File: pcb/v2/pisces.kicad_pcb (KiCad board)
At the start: 2 copper layers, 154.9 x 66 mm, 60 parts, among them J1 USB_B_Micro, J2 AudioJack4, SW1 SW_PUSH, SW10 SW_PUSH, SW11 SW_PUSH, SW12 SW_PUSH, SW13 SW_PUSH, SW14 SW_PUSH, SW15 SW_PUSH, SW16 SW_PUSH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

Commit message: Done with routing
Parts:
- moved C3 98.5 mm to (169.4, 58.1), turned to 180 degrees
- moved R2 96.2 mm to (159.1, 48.3), turned to 90 degrees
- moved R1 95.3 mm to (161.2, 48.3), turned to 90 degrees
- moved C2 90.4 mm to (158.7, 68.5)
- moved C1 89.6 mm to (158.7, 60.5), turned to 180 degrees
- moved C6 89.3 mm to (163.6, 60.5), turned to 180 degrees
- moved R3 88.7 mm to (174.0, 58.3)
- moved U1 88.6 mm to (167.7, 66.9)
- moved F1 85.0 mm to (156.8, 48.7), turned to 90 degrees
- moved C4 81.0 mm to (164.3, 58.4), turned to 180 degrees
- moved J1 76.9 mm to (160.5, 41.5), turned to 180 degrees
- moved C5 75.5 mm to (158.7, 71.4), turned to 180 degrees
- moved R4 74.1 mm to (168.8, 75.2), turned to 180 degrees
- moved Y1 50.1 mm to (157.5, 64.3), turned to 180 degrees
- moved RSTSW1 18.0 mm to (172.8, 55.4)
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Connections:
- U1 pad 10: col0 -> Net-(U1-Pad10)
- U1 pad 11: col1 -> Net-(U1-Pad11)
- U1 pad 12: col2 -> Net-(U1-Pad12)
- U1 pad 14: col3 -> row1
- U1 pad 15: col4 -> col0
- U1 pad 16: col5 -> col1
- U1 pad 17: Net-(U1-Pad17) -> col2
- U1 pad 18: Net-(U1-Pad18) -> col3
- U1 pad 19: Net-(U1-Pad19) -> col4
- U1 pad 20: Net-(U1-Pad20) -> col5
- U1 pad 21: Net-(U1-Pad21) -> col6
- U1 pad 22: Net-(U1-Pad22) -> row2
- U1 pad 23: row2 -> data
- U1 pad 25: row1 -> Net-(U1-Pad25)
- U1 pad 8: data -> Net-(U1-Pad8)
- U1 pad 9: col6 -> Net-(U1-Pad9)
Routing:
- net col0: track 53.1 -> 196.1 mm
- net col1: track 53.3 -> 177.6 mm
- net col2: track 53.3 -> 158.5 mm
- net col3: track 53.6 -> 140.1 mm
- net VCC: track 0.00 -> 79.0 mm, vias 0 -> 2
- net col4: track 53.3 -> 122.4 mm
- net col5: track 53.6 -> 104.3 mm
- net GND: track 0.00 -> 48.1 mm, vias 0 -> 1
- net col6: track 4.96 -> 38.4 mm
- net data: track 0.00 -> 30.0 mm, vias 0 -> 1
- net row2: track 131.1 -> 161.0 mm
- net row1: track 109.7 -> 137.7 mm
- net row0: track 109.7 -> 131.1 mm, vias 6 -> 7
- net d_m: track 0.00 -> 16.5 mm
- net d_p: track 0.00 -> 15.9 mm
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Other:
- board size 154.9 x 66 mm -> 138.4 x 61 mm

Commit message: PCB almost there...
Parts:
- added RR1: 10k, Resistor_SMD:R_0805_2012Metric_Pad1.20x1.40mm_HandSolder, F.Cu at (162.2, 75.2)
- moved R4 2.35 mm to (166.4, 75.2)
- moved J1 0.25 mm to (160.5, 41.7)
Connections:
- U1 pad 23: data -> Net-(U1-Pad23)
- U1 pad 8: Net-(U1-Pad8) -> data
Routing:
- net data: track 30.0 -> 38.6 mm, vias 1 -> 2
- net GND: track 48.1 -> 54.8 mm, vias 1 -> 3
- net Net-(RR1-Pad1): track 0.00 -> 6.42 mm
- net col0: track 196.1 -> 190.4 mm
- net col1: track 177.6 -> 172.0 mm
- net row1: track 137.7 -> 132.7 mm
- net col6: track 38.4 -> 34.1 mm
- net col5: track 104.3 -> 100.2 mm
- net col2: track 158.5 -> 154.6 mm
- net col4: track 122.4 -> 118.5 mm
- net col3: track 140.1 -> 136.3 mm
- net Net-(J2-PadS): track 6.53 -> 7.58 mm
- net row2: track 161.0 -> 160.2 mm
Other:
- board size 138.4 x 61 mm -> 137.8 x 60.1 mm

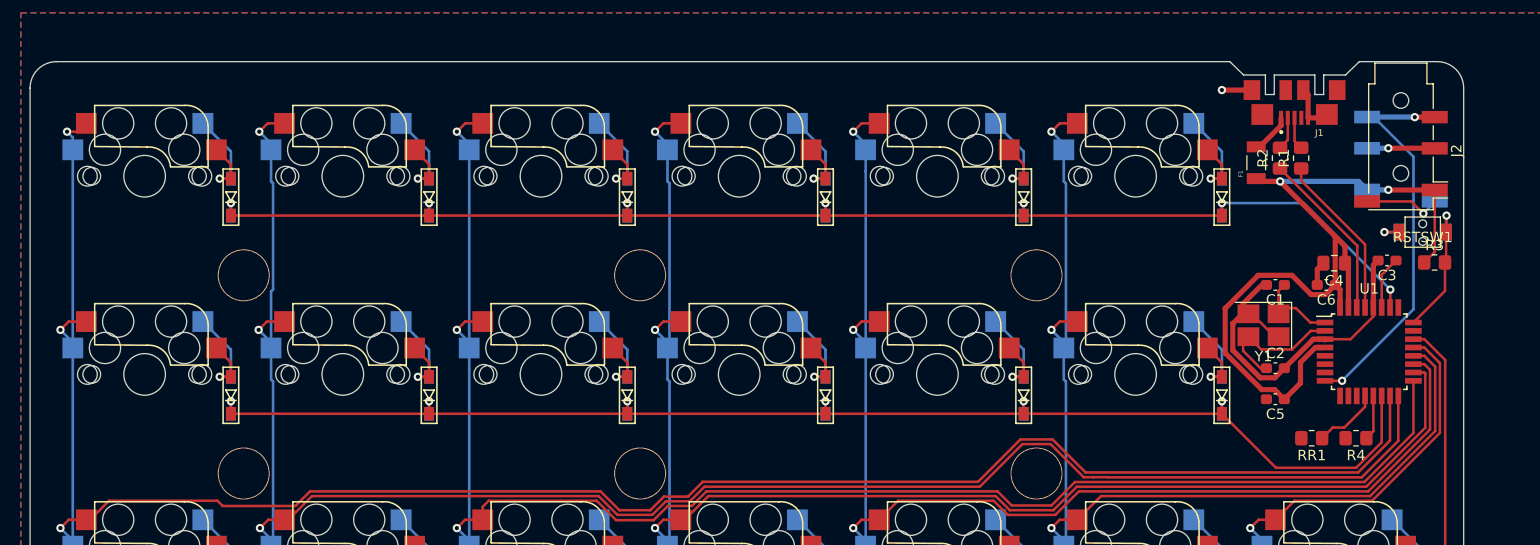
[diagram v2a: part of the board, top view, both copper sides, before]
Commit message: Added signiture on PCB
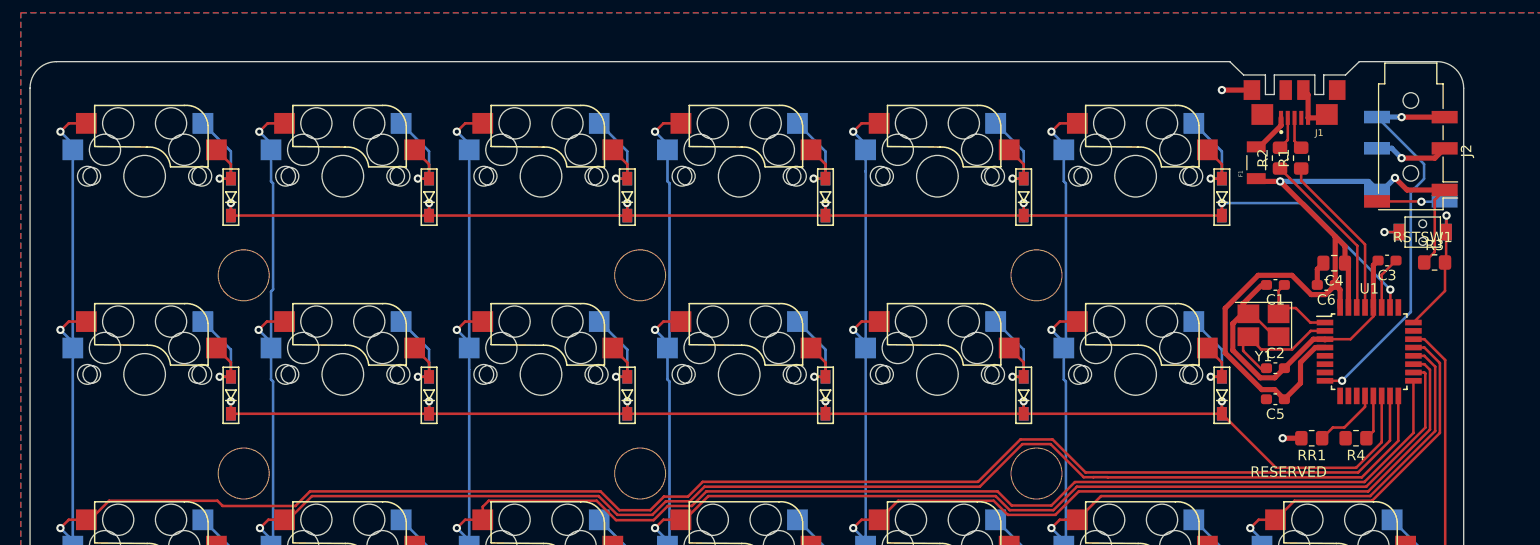
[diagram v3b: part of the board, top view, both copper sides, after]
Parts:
- moved J2 0.95 mm to (171.7, 47.5)
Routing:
- net GND: track 54.8 -> 57.4 mm, vias 3 -> 4
- net VCC: track 79.0 -> 81.3 mm
- net Net-(J2-PadS): track 7.58 -> 6.67 mm
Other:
- board text added: "RESERVED"
- board text added: "pisces v2.0 by knaruo"
